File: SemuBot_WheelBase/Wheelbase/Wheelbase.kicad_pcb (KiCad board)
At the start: 2 copper layers, 100 x 80 mm, 120 parts, among them IC1 DRV8353FSRTAR, IC2 DRV8353FSRTAR, IC3 DRV8353FSRTAR, J1 10155435-00011LF, J10 B5B-XH-A_LF__SN_, J11 B5B-XH-A_LF__SN_, J12 B5B-XH-A_LF__SN_, J13 MTSW-104-09-L-S-400, J14 XT30PW-M, J15 MTSW-104-09-L-S-400, J2 MTSW-102-09-L-S-400, J3 MR30PW-M, J4 B5B-XH-A_LF__SN_, J5 B5B-XH-A_LF__SN_, J6 B5B-XH-A_LF__SN_, J7 MR30PW-M, J8 MR30PW-M, J9 DS1013-10SSIB1, Q1 AON7262E, Q10 AON7262E, Q11 AON7262E, Q12 AON7262E, Q13 AON7262E, Q14 AON7262E, Q15 AON7262E, Q19 AON7262E, Q2 AON7262E, Q20 AON7262E, Q21 AON7262E, Q3 AON7262E, Q4 AON7262E, Q5 AON7262E, Q6 AON7262E, Q7 AON7262E, Q8 AON7262E, Q9 AON7262E, U1 STM32F303RET6, U5 RT9013-33GB, Y2 X322516MLB4SI

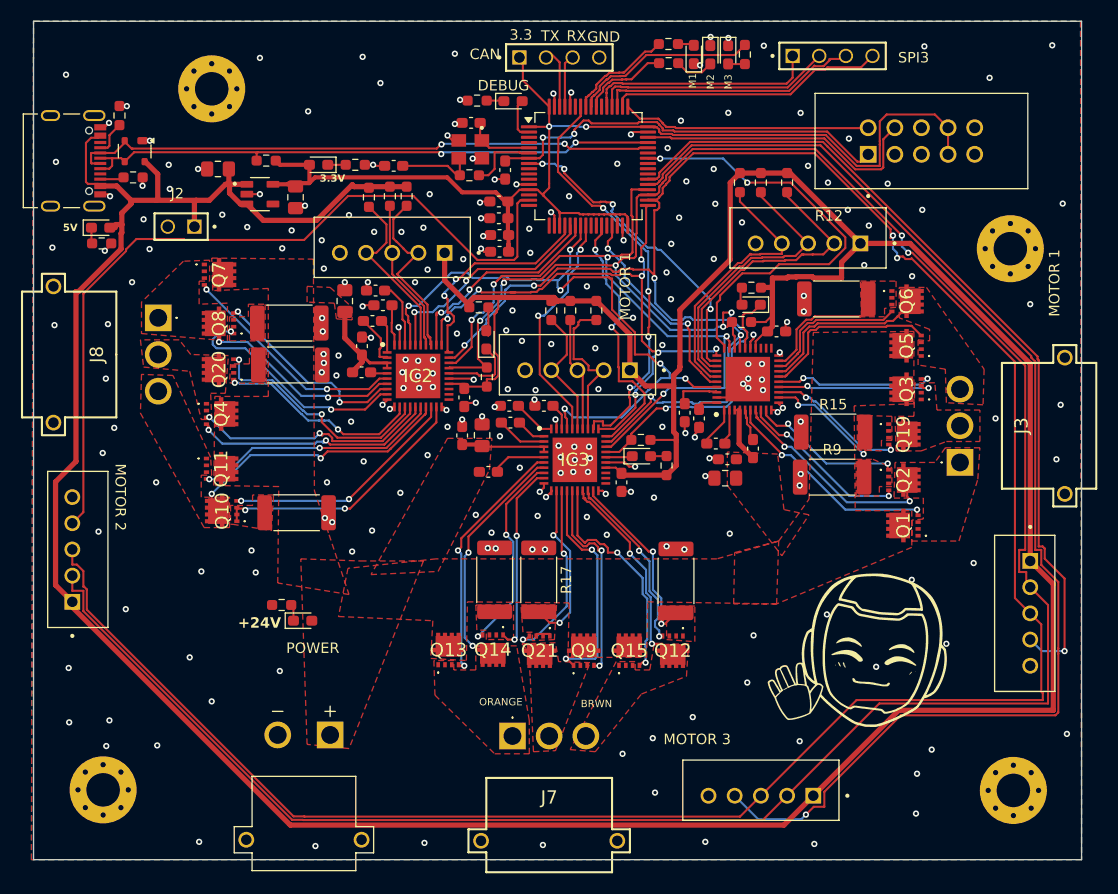
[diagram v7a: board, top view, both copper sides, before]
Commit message: SPI version update
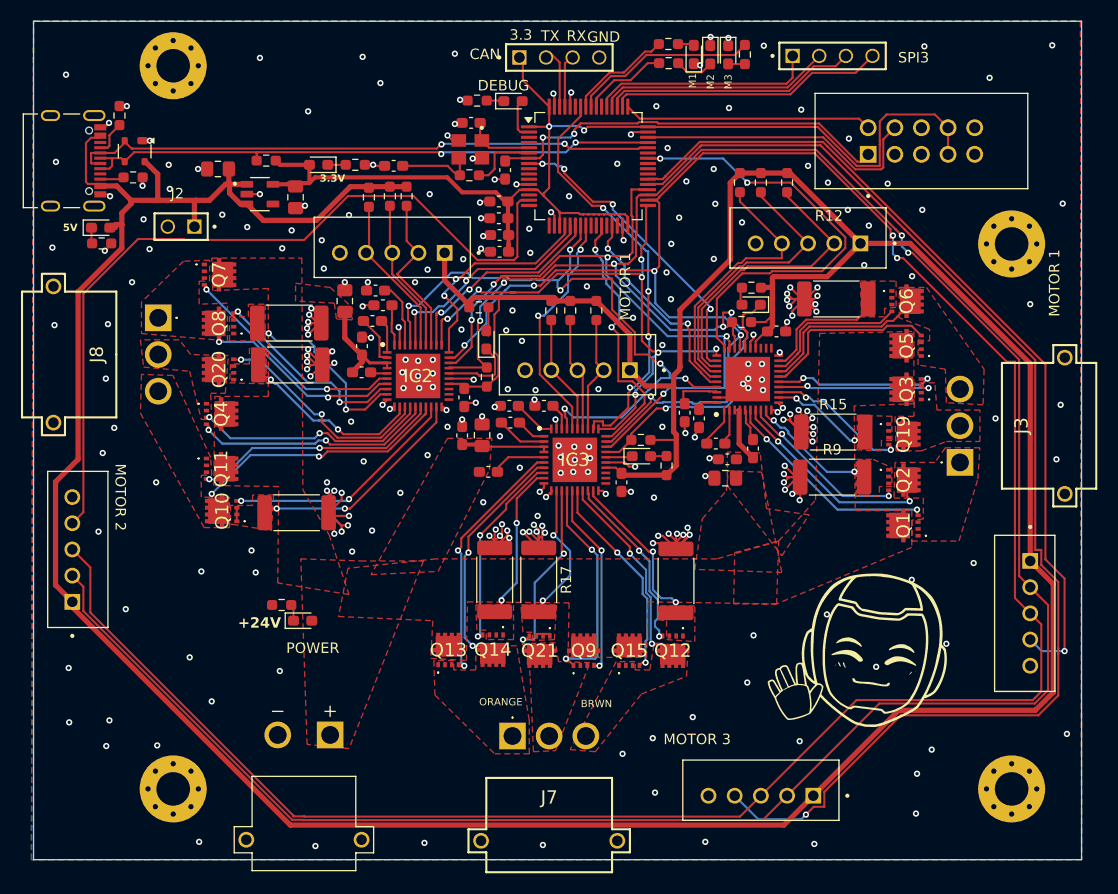
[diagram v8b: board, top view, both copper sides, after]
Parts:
- moved H1 6.69 mm to (115.0, 134.0)
- moved H4 4.28 mm to (115.0, 65.0)
- moved H3 0.47 mm to (195.0, 82.0)
- moved H2 0.22 mm to (195.0, 134.0)
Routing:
- net GND: track 61.7 -> 176.0 mm, vias 235 -> 267
- net /Motor_2/SPA: track 22.7 -> 18.2 mm
- net /Motor_3/HAL_1: track 15.4 -> 11.3 mm
- net /SPI_DATA: track 269.0 -> 265.8 mm
- net /Motor_3/SPA: track 18.2 -> 15.1 mm
- net /Motor_2/HAL_3: track 17.4 -> 14.7 mm
- net /SPI_CLK: track 259.8 -> 257.1 mm
- net +5V: track 378.7 -> 376.1 mm
- net /Motor_3/SPB: track 17.6 -> 15.1 mm
- net /Motor_2/SPC: track 25.3 -> 22.8 mm
- net /Motor_1/SPB: track 12.8 -> 10.3 mm
- net /Motor_2/SPB: track 19.7 -> 17.3 mm
- net /Motor_1/SPA: track 14.9 -> 12.6 mm
- net /Motor_3/GHC: track 21.7 -> 19.9 mm
- net /Motor_3/SPC: track 17.5 -> 15.7 mm
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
